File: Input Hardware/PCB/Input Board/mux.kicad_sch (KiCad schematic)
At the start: 36 parts, among them U701 ADA4891, U702 CD4051B, U703 CD4051B

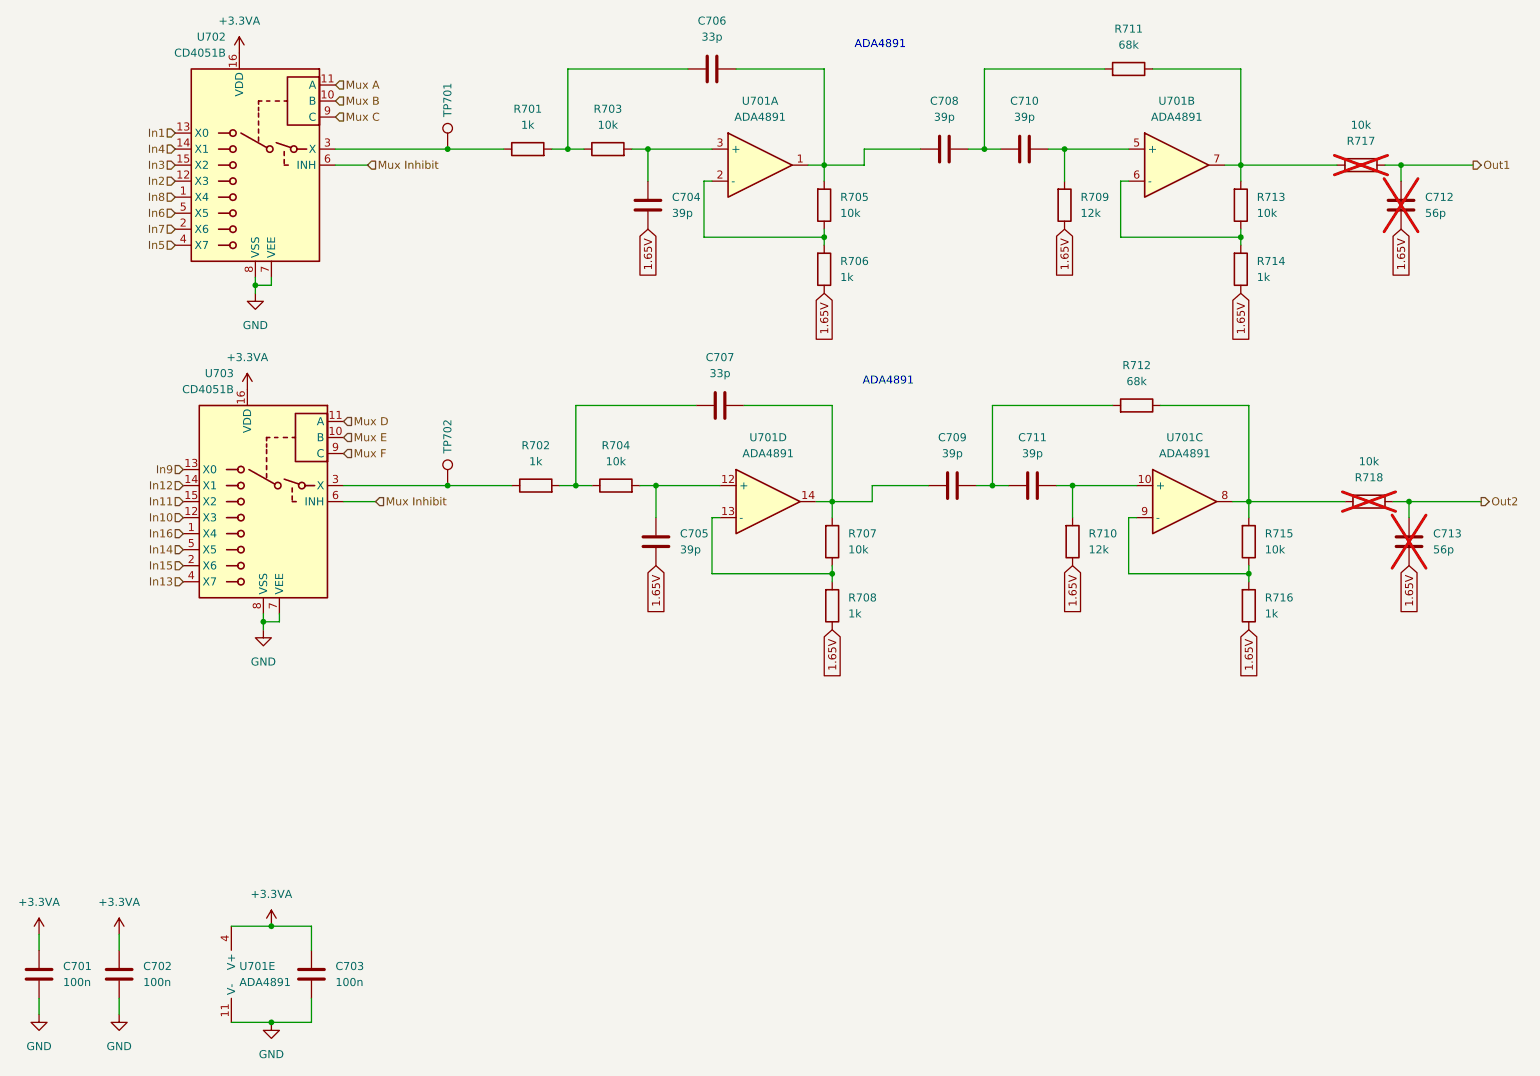
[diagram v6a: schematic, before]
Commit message: add bias resistor, fix LED polarity
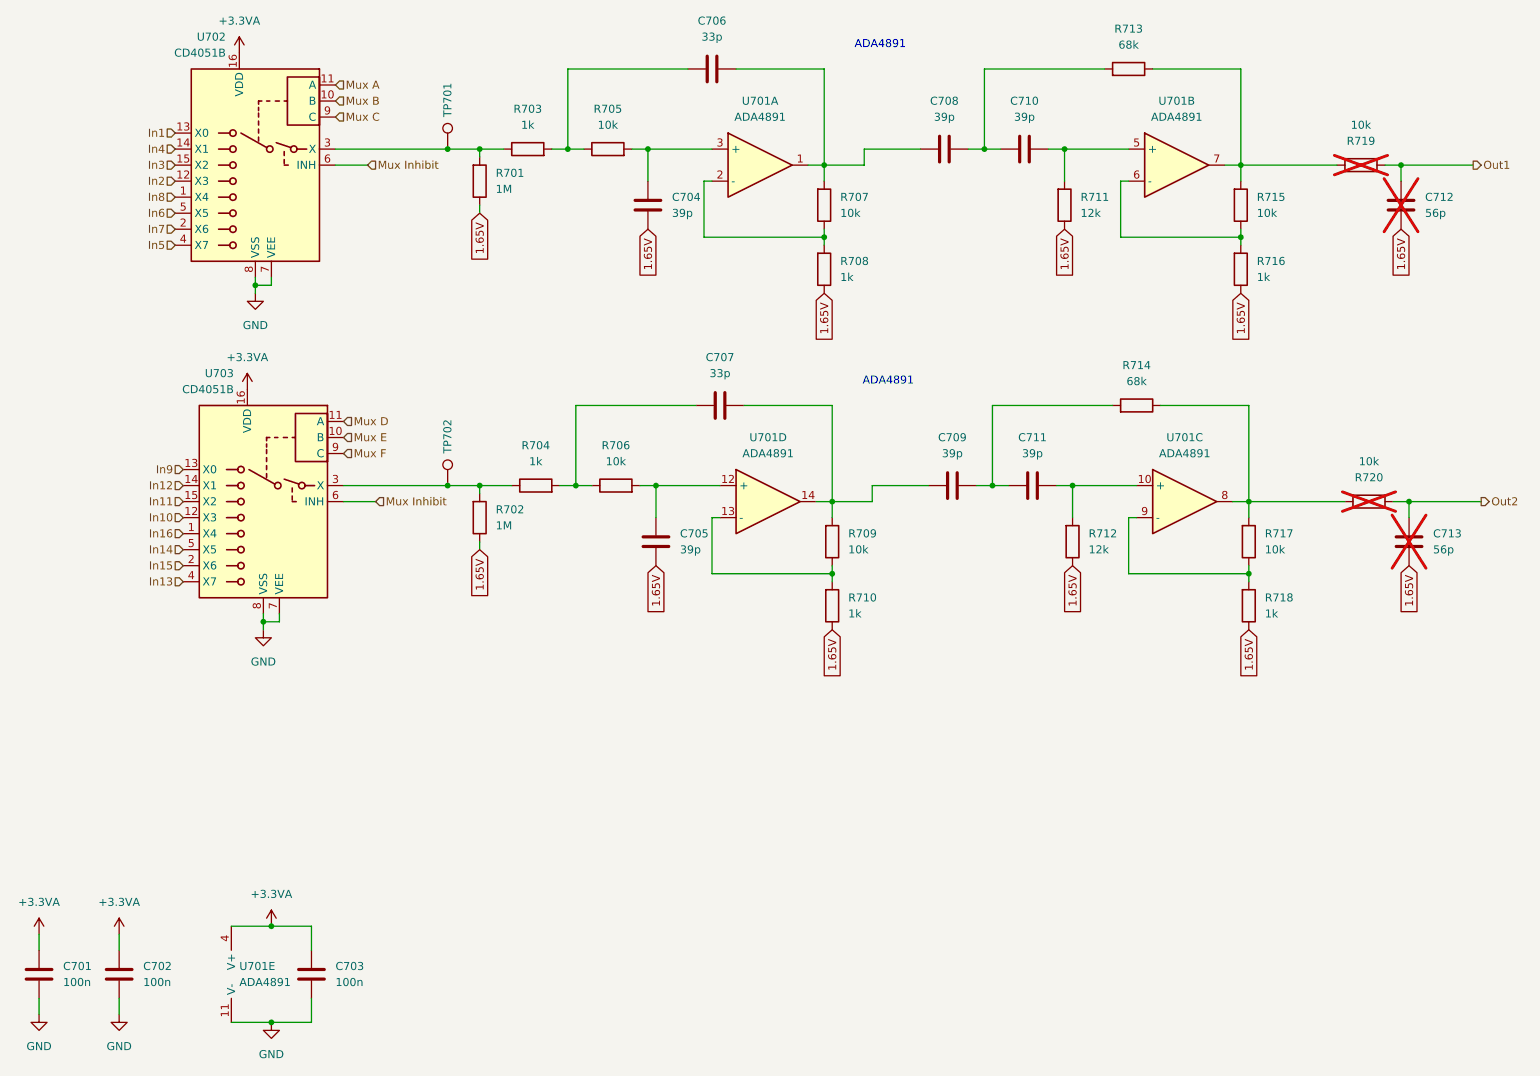
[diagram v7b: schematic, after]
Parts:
- added R701, R702: 1M, Resistor_SMD:R_0603_1608Metric, symbol Device:R
- renumbered R701 to R703, R702 to R704, R703 to R705, R704 to R706, R705 to R707, R706 to R708, R707 to R709, R708 to R710, R709 to R711, R710 to R712, R711 to R713, R712 to R714, R713 to R715, R714 to R716, R715 to R717, R716 to R718, R717 to R719, R718 to R720
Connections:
- net 1.65V: now also R701.1, R702.1
- net at R703.1, TP701.1, U702.3 (X): now also R701.2
- net at R704.1, TP702.1, U703.3 (X): now also R702.2
